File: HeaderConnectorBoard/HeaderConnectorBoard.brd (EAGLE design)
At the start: 31.1 x 67.9 mm, 2 parts

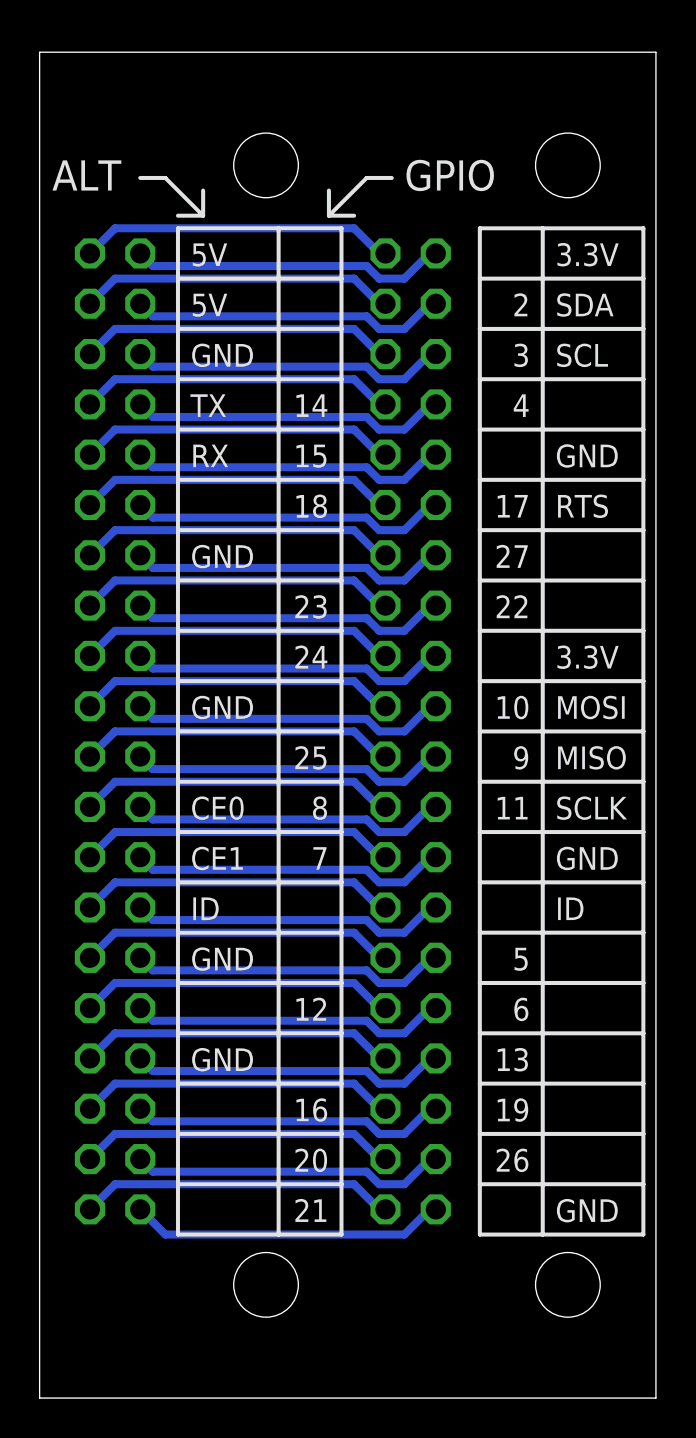
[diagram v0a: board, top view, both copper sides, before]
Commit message: lid connector - Readjust mounting holes.  Rev-01a.
adjustments to allow screw head clearance for board headers, and to clear silkscreen.
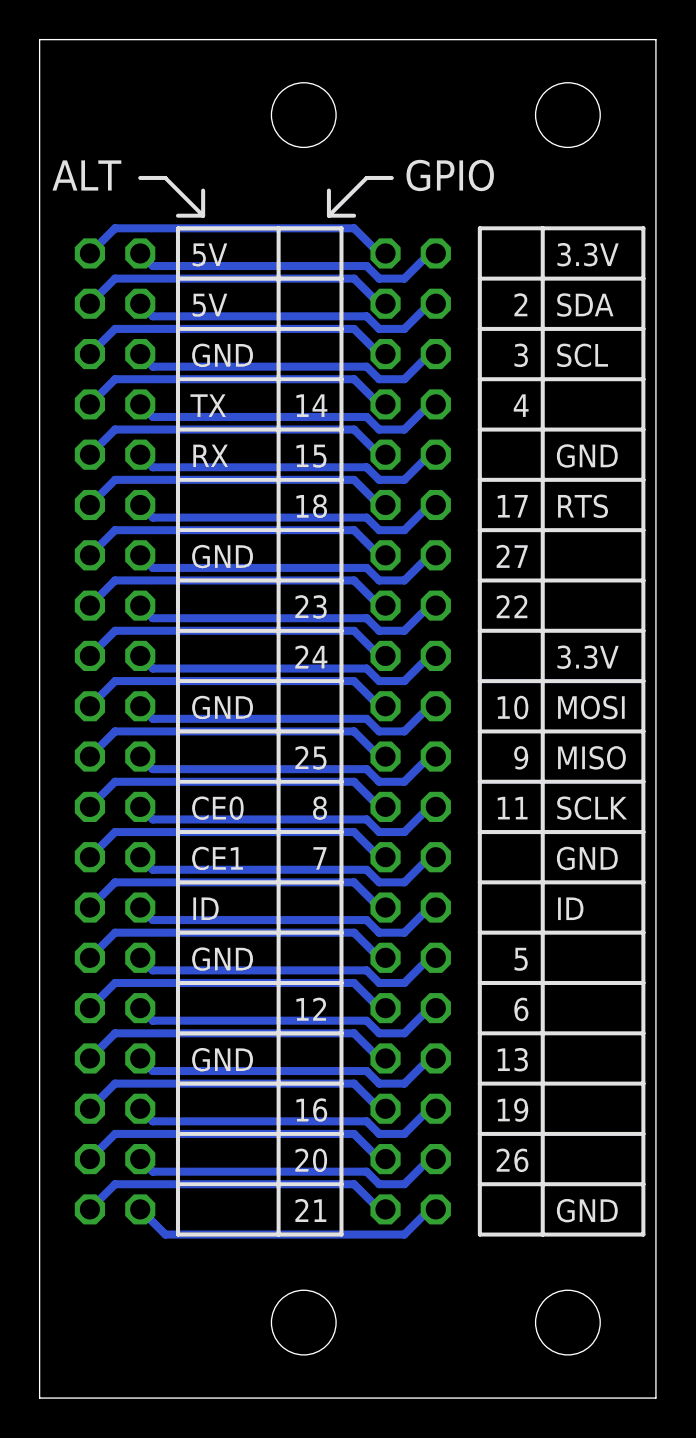
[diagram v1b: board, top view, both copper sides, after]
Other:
- board size 31.1 x 67.9 mm -> 31.1 x 68.6 mm
- board text added: "Rev-01a (c) 2015 RaspberrySTEM"
- board text removed: "Rev-00a (c) 2015 RaspberrySTEM"
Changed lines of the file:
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@@
 <plain>
 <wire x1="0" y1="0" x2="31.115" y2="0" width="0" layer="20"/>
-<wire x1="31.115" y1="0" x2="31.115" y2="67.935" width="0" layer="20"/>
+<wire x1="31.115" y1="0" x2="31.115" y2="68.57" width="0" layer="20"/>
 <text x="26.035" y="57.15" size="1.143" layer="21" font="vector">3.3V</text>
 <text x="24.765" y="54.61" size="1.143" layer="21" font="vector" align="bottom-right">2</text>
@@
 <text x="14.605" y="26.67" size="1.143" layer="21" font="vector" align="bottom-right">7</text>
 <text x="7.62" y="52.07" size="1.143" layer="21" font="vector">GND</text>
-<hole x="11.43" y="5.715" drill="3.2639"/>
-<hole x="26.67" y="5.715" drill="3.2639"/>
-<wire x1="0" y1="67.935" x2="0" y2="0" width="0" layer="20"/>
+<hole x="13.335" y="3.81" drill="3.2639"/>
+<hole x="26.67" y="3.81" drill="3.2639"/>
+<wire x1="0" y1="68.57" x2="0" y2="0" width="0" layer="20"/>
 <wire x1="25.4" y1="59.055" x2="30.48" y2="59.055" width="0.2032" layer="21"/>
 <wire x1="30.48" y1="59.055" x2="30.48" y2="56.515" width="0.2032" layer="21"/>
@@
 <text x="26.035" y="8.89" size="1.143" layer="21" font="vector">GND</text>
 <text x="26.035" y="24.13" size="1.143" layer="21" font="vector">ID</text>
-<text x="11.43" y="38.735" size="1.778" layer="22" font="vector" rot="MR270" align="center">Rev-00a
+<text x="11.43" y="38.735" size="1.778" layer="22" font="vector" rot="MR270" align="center">Rev-01a
 (c) 2015 RaspberrySTEM</text>
-<hole x="11.43" y="62.23" drill="3.2639"/>
-<hole x="26.67" y="62.23" drill="3.2639"/>
+<hole x="13.335" y="64.77" drill="3.2639"/>
+<hole x="26.67" y="64.77" drill="3.2639"/>
 <polygon width="0.0254" layer="22">
 <vertex x="29.8958" y="38.7096"/>
@@
 <vertex x="27.1526" y="36.957"/>
 </polygon>
-<wire x1="0" y1="67.945" x2="31.115" y2="67.945" width="0" layer="20"/>
+<wire x1="0" y1="68.58" x2="31.115" y2="68.58" width="0" layer="20"/>
 <text x="18.415" y="60.96" size="1.524" layer="21" font="vector">GPIO</text>
 <text x="0.635" y="60.96" size="1.524" layer="21" font="vector">ALT</text>
